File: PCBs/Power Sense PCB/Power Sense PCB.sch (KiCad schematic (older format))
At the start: 84 parts, among them J1 Jack-DC, J10 Test Conn, J2 PWR_INV, J3 PWR_INPUT, J4 PHASE_A_INV, J5 PHASE_A_MOTOR, J6 PHASE_B_INV, J7 PHASE_B_MOTOR, J8 PHASE_C_INV, J9 PHASE_C_MOTOR, U1 INA240A1D, U2 INA240A1D, U3 INA240A1D, U4 INA240A1D

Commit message: Layout + Routing
- Added 5V LED indicatior
- Added 330uF bulk cap on 5V rail
- Changed 8pin to 9pin header (added ground)
- Completed all layout and routing!
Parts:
- added C17: 330uF, Capacitors_THT:CP_Radial_D8.0mm_P3.50mm, symbol Device:CP1
- added D1: RED, LEDs:LED_0603, symbol Device:LED
- added R20: 330, Resistors_SMD:R_0603, symbol Device:R_Small_US
- J10: footprint Pin_Headers:Pin_Header_Straight_1x08_Pitch2.54mm -> Pin_Headers:Pin_Header_Straight_1x09_Pitch2.54mm; symbol Connector_Generic:Conn_01x08 -> Connector_Generic:Conn_01x09; Digikey 961108-6404-AR -> 3M9457-09-ND
- NT1, NT2, NT3, NT4, NT5, NT6, NT7, NT8: footprint NetTies:NetTie-2_SMD_Pad0.5mm -> Power Sense PCB:NetTie-2_SMD_Pad0.25mm
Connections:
- net +5V: now also C17.1, D1.2 (A)
- net GND: now also J10.9 (Pin_9), C17.2, R20.2
- new net: D1.1 (K), R20.1
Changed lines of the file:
@@
 F 0 "NT4" V 3950 1919 50  0000 L CNN
 F 1 "Net-Tie_2" V 3995 1919 50  0001 L CNN
-F 2 "NetTies:NetTie-2_SMD_Pad0.5mm" H 3950 1875 50  0001 C CNN
+F 2 "Power Sense PCB:NetTie-2_SMD_Pad0.25mm" H 3950 1875 50  0001 C CNN
 F 3 "~" H 3950 1875 50  0001 C CNN
 	1    3950 1875
@@
 F 0 "NT3" V 3350 1919 50  0000 L CNN
 F 1 "Net-Tie_2" V 3395 1919 50  0001 L CNN
-F 2 "NetTies:NetTie-2_SMD_Pad0.5mm" H 3350 1875 50  0001 C CNN
+F 2 "Power Sense PCB:NetTie-2_SMD_Pad0.25mm" H 3350 1875 50  0001 C CNN
 F 3 "~" H 3350 1875 50  0001 C CNN
 	1    3350 1875
@@
 	1400 1150 1625 1150
 Wire Wire Line
-	1625 1150 1625 975
+	1625 1150 1625 1075
 $Comp
 L power:+5V #PWR0103
@@
 	1400 1350 1625 1350
 Wire Wire Line
-	1625 1350 1625 1500
+	1625 1350 1625 1450
 $Comp
 L power:GND #PWR0104
@@
 F 0 "NT6" V 3925 4019 50  0000 L CNN
 F 1 "Net-Tie_2" V 3970 4019 50  0001 L CNN
-F 2 "NetTies:NetTie-2_SMD_Pad0.5mm" H 3925 3975 50  0001 C CNN
+F 2 "Power Sense PCB:NetTie-2_SMD_Pad0.25mm" H 3925 3975 50  0001 C CNN
 F 3 "~" H 3925 3975 50  0001 C CNN
 	1    3925 3975
@@
 F 0 "NT5" V 3325 4019 50  0000 L CNN
 F 1 "Net-Tie_2" V 3370 4019 50  0001 L CNN
-F 2 "NetTies:NetTie-2_SMD_Pad0.5mm" H 3325 3975 50  0001 C CNN
+F 2 "Power Sense PCB:NetTie-2_SMD_Pad0.25mm" H 3325 3975 50  0001 C CNN
 F 3 "~" H 3325 3975 50  0001 C CNN
 	1    3325 3975
@@
 F 0 "NT8" V 3900 6094 50  0000 L CNN
 F 1 "Net-Tie_2" V 3945 6094 50  0001 L CNN
-F 2 "NetTies:NetTie-2_SMD_Pad0.5mm" H 3900 6050 50  0001 C CNN
+F 2 "Power Sense PCB:NetTie-2_SMD_Pad0.25mm" H 3900 6050 50  0001 C CNN
 F 3 "~" H 3900 6050 50  0001 C CNN
 	1    3900 6050
@@
 F 0 "NT7" V 3300 6094 50  0000 L CNN
 F 1 "Net-Tie_2" V 3345 6094 50  0001 L CNN
-F 2 "NetTies:NetTie-2_SMD_Pad0.5mm" H 3300 6050 50  0001 C CNN
+F 2 "Power Sense PCB:NetTie-2_SMD_Pad0.25mm" H 3300 6050 50  0001 C CNN
 F 3 "~" H 3300 6050 50  0001 C CNN
 	1    3300 6050
@@
 F 0 "NT2" V 8175 1844 50  0000 L CNN
 F 1 "Net-Tie_2" V 8220 1844 50  0001 L CNN
-F 2 "NetTies:NetTie-2_SMD_Pad0.5mm" H 8175 1800 50  0001 C CNN
+F 2 "Power Sense PCB:NetTie-2_SMD_Pad0.25mm" H 8175 1800 50  0001 C CNN
 F 3 "~" H 8175 1800 50  0001 C CNN
 	1    8175 1800
@@
 F 0 "NT1" V 7575 1844 50  0000 L CNN
 F 1 "Net-Tie_2" V 7620 1844 50  0001 L CNN
-F 2 "NetTies:NetTie-2_SMD_Pad0.5mm" H 7575 1800 50  0001 C CNN
+F 2 "Power Sense PCB:NetTie-2_SMD_Pad0.25mm" H 7575 1800 50  0001 C CNN
 F 3 "~" H 7575 1800 50  0001 C CNN
 	1    7575 1800
@@
 Should be approx the same\nvoltage as the real motor neutral, \nsince phases are close to balanced.
 $Comp
-L Connector_Generic:Conn_01x08 J10
+L Connector_Generic:Conn_01x09 J10
 U 1 1 5E4D3815
 P 10550 3700
-F 0 "J10" H 10475 4100 50  0000 L CNN
+F 0 "J10" H 10500 4225 50  0000 L CNN
 F 1 "Test Conn" H 10475 3200 50  0000 L CNN
-F 2 "Pin_Headers:Pin_Header_Straight_1x08_Pitch2.54mm" H 10550 3700 50  0001 C CNN
+F 2 "Pin_Headers:Pin_Header_Straight_1x09_Pitch2.54mm" H 10550 3700 50  0001 C CNN
 F 3 "~" H 10550 3700 50  0001 C CNN
-F 4 "961108-6404-AR" H 10550 3700 50  0001 C CNN "Digikey"
+F 4 "3M9457-09-ND" H 10550 3700 50  0001 C CNN "Digikey"
 	1    10550 3700
 	1    0    0    -1
 $EndComp
 Wire Wire Line
+	10350 3300 9825 3300
+Wire Wire Line
 	10350 3400 9825 3400
-Wire Wire Line
-	10350 3500 9825 3500
+Text Label 9825 3300 0    50   ~ 0
+V_BUS
 Text Label 9825 3400 0    50   ~ 0
-V_BUS
-Text Label 9825 3500 0    50   ~ 0
 I_BUS
 Wire Wire Line
-	9825 3600 10350 3600
+	9825 3500 10350 3500
+Wire Wire Line
+	10350 3600 9825 3600
 Wire Wire Line
 	10350 3700 9825 3700
@@
 Wire Wire Line
 	10350 4000 9825 4000
-Wire Wire Line
-	10350 4100 9825 4100
 $Comp
 L Device:C_Small C7
@@
 Wire Wire Line
 	6250 3900 7200 3900
+Text Label 9825 3500 0    50   ~ 0
+V_PHASE_A
 Text Label 9825 3600 0    50   ~ 0
-V_PHASE_A
+V_PHASE_B
 Text Label 9825 3700 0    50   ~ 0
-V_PHASE_B
+V_PHASE_C
+Text Label 9825 3900 0    50   ~ 0
+I_PHASE_B
 Text Label 9825 3800 0    50   ~ 0
-V_PHASE_C
+I_PHASE_A
 Text Label 9825 4000 0    50   ~ 0
-I_PHASE_B
-Text Label 9825 3900 0    50   ~ 0
-I_PHASE_A
-Text Label 9825 4100 0    50   ~ 0
 I_PHASE_C
-Text Notes 9550 4375 0    50   ~ 0
+Text Notes 9525 4600 0    50   ~ 0
 For data aquistion via Arduino or similar.
-Text Notes 10025 4500 0    50   ~ 0
+Text Notes 10000 4725 0    50   ~ 0
 All signals 0-5V
 $Comp
@@
 Wire Wire Line
 	7125 1625 7575 1625
+$Comp
+L Device:CP1 C17
+U 1 1 5E383FE4
+P 1800 1250
+F 0 "C17" H 1915 1296 50  0000 L CNN
+F 1 "330uF" H 1915 1205 50  0000 L CNN
+F 2 "Capacitors_THT:CP_Radial_D8.0mm_P3.50mm" H 1800 1250 50  0001 C CNN
+F 3 "~" H 1800 1250 50  0001 C CNN
+F 4 "493-15427-ND" H 1800 1250 50  0001 C CNN "Digikey"
+	1    1800 1250
+	1    0    0    -1
+$EndComp
+Wire Wire Line
+	1625 1075 1800 1075
+Wire Wire Line
+	1800 1075 1800 1100
+Connection ~ 1625 1075
+Wire Wire Line
+	1625 1075 1625 975
+Wire Wire Line
+	1800 1400 1800 1450
+Wire Wire Line
+	1800 1450 1625 1450
+Connection ~ 1625 1450
+Wire Wire Line
+	1625 1450 1625 1500
+$Comp
+L Device:LED D1
+U 1 1 5E3AA4EA
+P 2225 1250
+F 0 "D1" V 2264 1132 50  0000 R CNN
+F 1 "RED" V 2173 1132 50  0000 R CNN
+F 2 "LEDs:LED_0603" H 2225 1250 50  0001 C CNN
+F 3 "~" H 2225 1250 50  0001 C CNN
+F 4 "160-1447-1-ND" V 2225 1250 50  0001 C CNN "Digikey"
+	1    2225 1250
+	0    -1   -1   0
+$EndComp
+Wire Wire Line
+	1800 1075 2225 1075
+Wire Wire Line
+	2225 1075 2225 1100
+Connection ~ 1800 1075
+$Comp
+L Device:R_Small_US R20
+U 1 1 5E3B8A0C
+P 2225 1550
+F 0 "R20" H 2293 1596 50  0000 L CNN
+F 1 "330" H 2293 1505 50  0000 L CNN
+F 2 "Resistors_SMD:R_0603" H 2225 1550 50  0001 C CNN
+F 3 "~" H 2225 1550 50  0001 C CNN
+F 4 "RHM330DCT-ND" H 2225 1550 50  0001 C CNN "Digikey"
+	1    2225 1550
+	1    0    0    -1
+$EndComp
+Wire Wire Line
+	2225 1400 2225 1450
+Wire Wire Line
+	2225 1650 2225 1725
+$Comp
+L power:GND #PWR01
+U 1 1 5E3D3814
+P 2225 1725
+F 0 "#PWR01" H 2225 1475 50  0001 C CNN
+F 1 "GND" H 2230 1552 50  0000 C CNN
+F 2 "" H 2225 1725 50  0001 C CNN
+F 3 "" H 2225 1725 50  0001 C CNN
+	1    2225 1725
+	1    0    0    -1
+$EndComp
+Wire Wire Line
+	10350 4100 10275 4100
+Wire Wire Line
+	10275 4100 10275 4175
+$Comp
+L power:GND #PWR?
+U 1 1 5E454E34
+P 10275 4175
+F 0 "#PWR?" H 10275 3925 50  0001 C CNN
+F 1 "GND" H 10280 4002 50  0000 C CNN
+F 2 "" H 10275 4175 50  0001 C CNN
+F 3 "" H 10275 4175 50  0001 C CNN
+	1    10275 4175
+	1    0    0    -1
+$EndComp
 $EndSCHEMATC

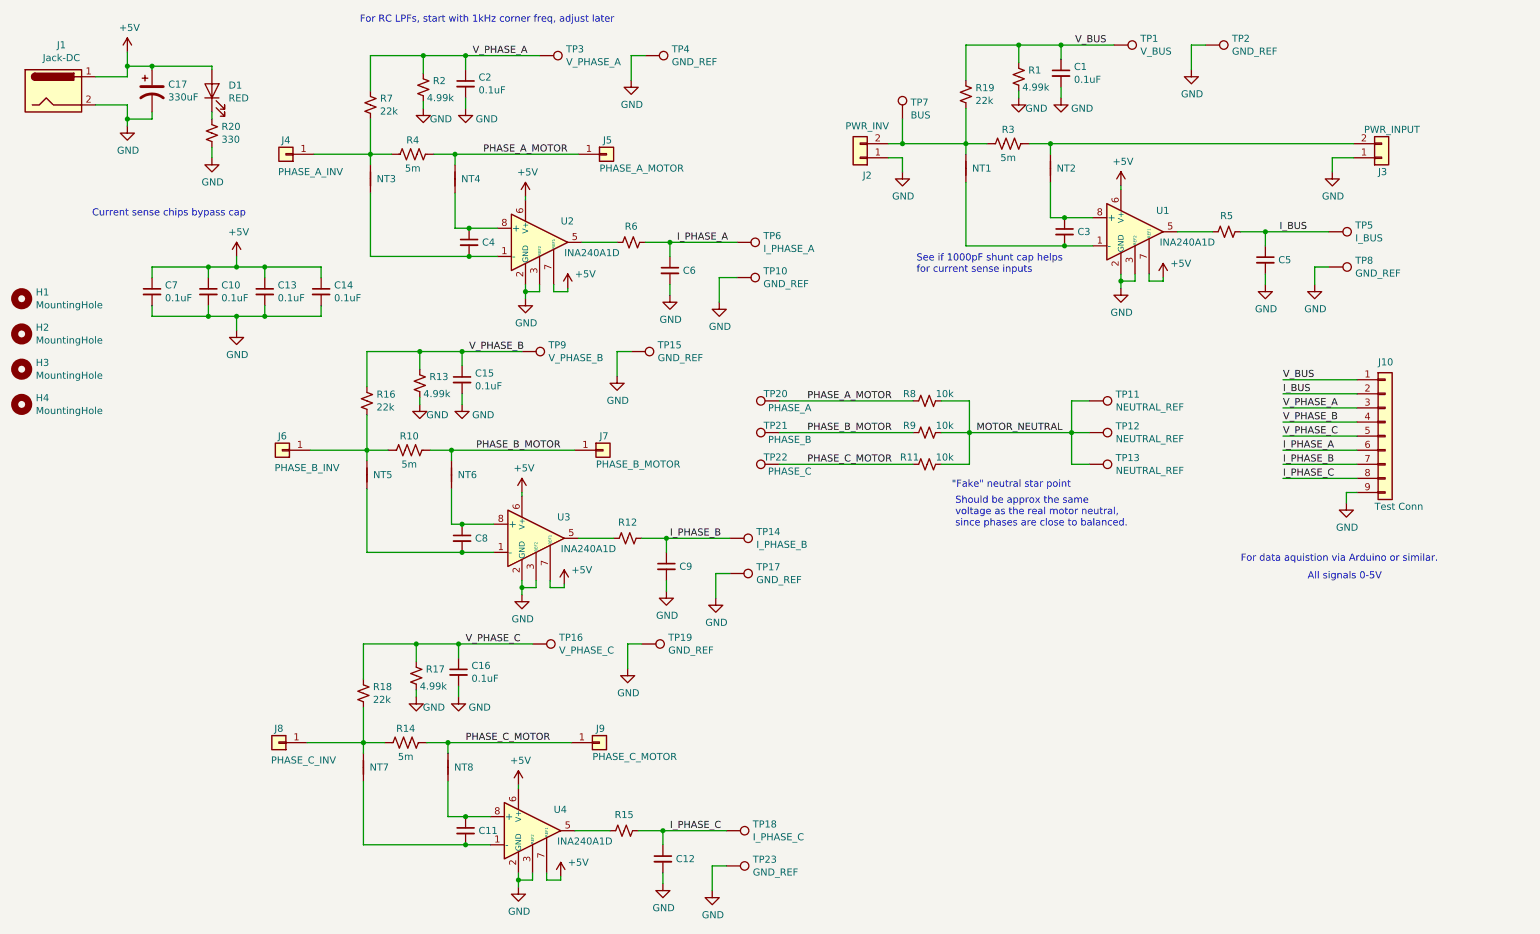
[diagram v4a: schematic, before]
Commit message: Gerbers and Small Changes
- Swapped Ref1 and Ref2 values based on datasheet (doesn't matter really)
- Updated Silkscreen
- Exported Gerbers
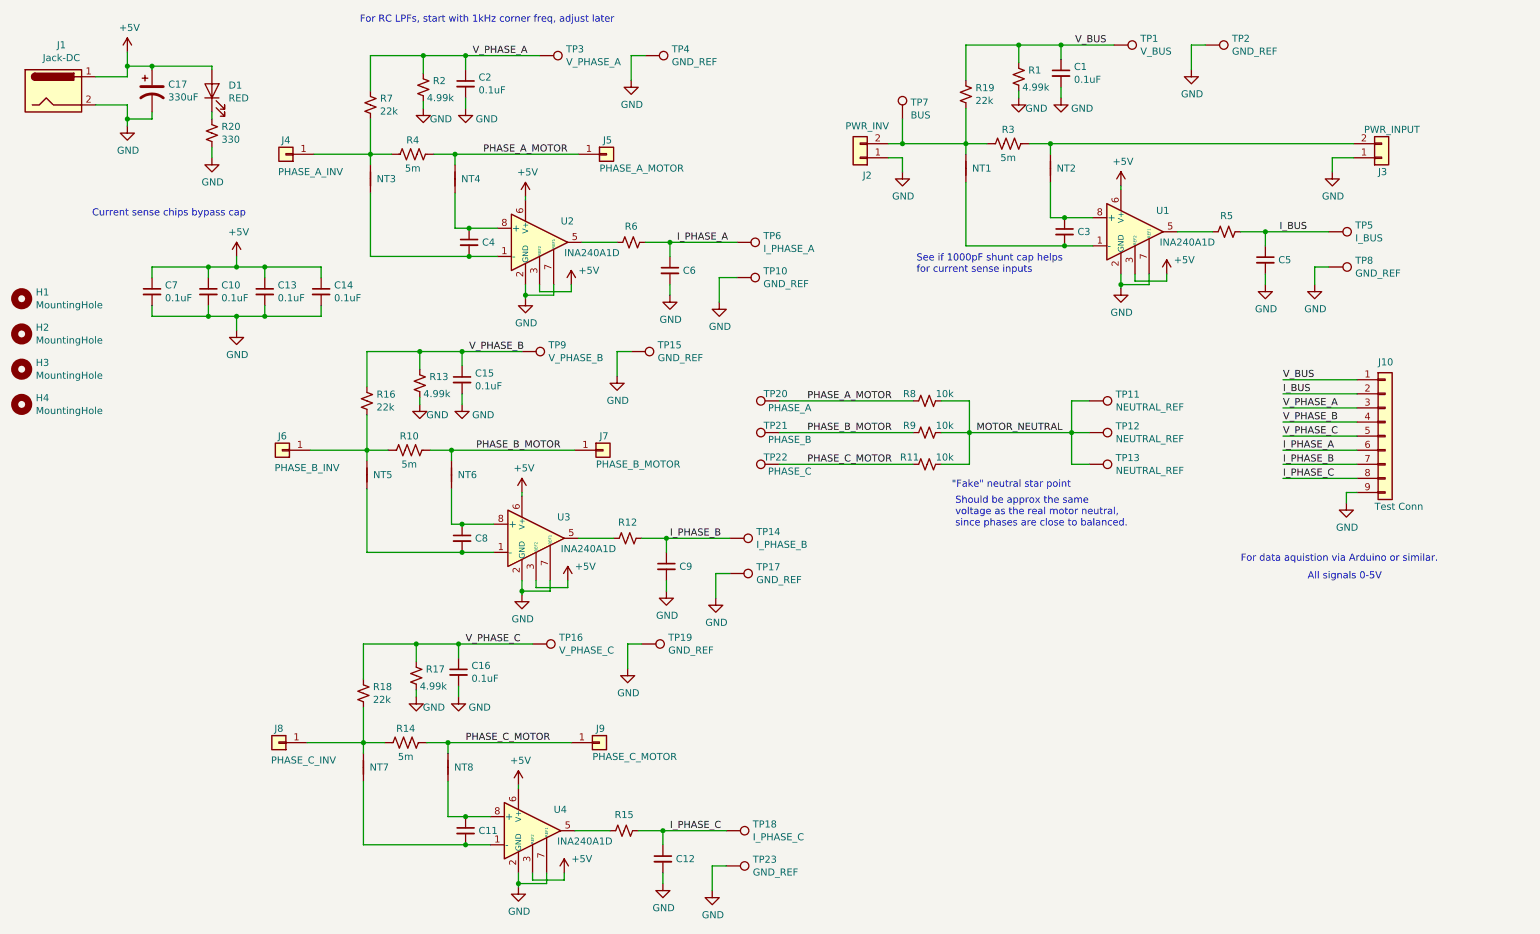
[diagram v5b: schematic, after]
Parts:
- U1, U2, U3, U4: footprint Housings_SOIC:SOIC-8-1EP_3.9x4.9mm_Pitch1.27mm -> Housings_SOIC:SOIC-8_3.9x4.9mm_Pitch1.27mm
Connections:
- net +5V: now also U1.3 (REF2), U2.3 (REF2), U3.3 (REF2), U4.3 (REF2); no longer U1.7 (REF1), U2.7 (REF1), U3.7 (REF1), U4.7 (REF1)
- net GND: now also U1.7 (REF1), U2.7 (REF1), U3.7 (REF1), U4.7 (REF1); no longer U1.3 (REF2), U2.3 (REF2), U3.3 (REF2), U4.3 (REF2)
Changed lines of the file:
@@
 Wire Wire Line
 	4450 2025 4450 2000
-Wire Wire Line
-	4450 2625 4450 2675
 $Comp
 L power:+5V #PWR0101
@@
 	1625 1350 1625 1450
 $Comp
-L power:GND #PWR0104
-U 1 1 5E2A5BAB
-P 4450 2725
-F 0 "#PWR0104" H 4450 2475 50  0001 C CNN
-F 1 "GND" H 4455 2552 50  0000 C CNN
-F 2 "" H 4450 2725 50  0001 C CNN
-F 3 "" H 4450 2725 50  0001 C CNN
-	1    4450 2725
-	1    0    0    -1
-$EndComp
-$Comp
 L power:GND #PWR0105
 U 1 1 5E2A60B1
@@
 F 3 "" H 1625 1500 50  0001 C CNN
 	1    1625 1500
-	1    0    0    -1
-$EndComp
-Wire Wire Line
-	4550 2625 4550 2675
-Wire Wire Line
-	4550 2675 4450 2675
-Connection ~ 4450 2675
-Wire Wire Line
-	4450 2675 4450 2725
-Wire Wire Line
-	4650 2625 4650 2675
-Wire Wire Line
-	4650 2675 4750 2675
-Wire Wire Line
-	4750 2675 4750 2650
-$Comp
-L power:+5V #PWR0106
-U 1 1 5E2A7916
-P 4750 2650
-F 0 "#PWR0106" H 4750 2500 50  0001 C CNN
-F 1 "+5V" H 4875 2750 50  0000 C CNN
-F 2 "" H 4750 2650 50  0001 C CNN
-F 3 "" H 4750 2650 50  0001 C CNN
-	1    4750 2650
 	1    0    0    -1
 $EndComp
@@
 Wire Wire Line
 	4425 4125 4425 4100
-Wire Wire Line
-	4425 4725 4425 4775
 $Comp
 L power:+5V #PWR0110
@@
 	0    1    1    0
 $EndComp
-$Comp
-L power:GND #PWR0112
-U 1 1 5E2DD8E3
-P 4425 4825
-F 0 "#PWR0112" H 4425 4575 50  0001 C CNN
-F 1 "GND" H 4430 4652 50  0000 C CNN
-F 2 "" H 4425 4825 50  0001 C CNN
-F 3 "" H 4425 4825 50  0001 C CNN
-	1    4425 4825
-	1    0    0    -1
-$EndComp
-Wire Wire Line
-	4525 4725 4525 4775
-Wire Wire Line
-	4525 4775 4425 4775
-Connection ~ 4425 4775
-Wire Wire Line
-	4425 4775 4425 4825
-Wire Wire Line
-	4625 4725 4625 4775
-Wire Wire Line
-	4625 4775 4725 4775
-Wire Wire Line
-	4725 4775 4725 4750
-$Comp
-L power:+5V #PWR0113
-U 1 1 5E2DD8F0
-P 4725 4750
-F 0 "#PWR0113" H 4725 4600 50  0001 C CNN
-F 1 "+5V" H 4850 4850 50  0000 C CNN
-F 2 "" H 4725 4750 50  0001 C CNN
-F 3 "" H 4725 4750 50  0001 C CNN
-	1    4725 4750
-	1    0    0    -1
-$EndComp
 Wire Wire Line
 	2925 3800 3325 3800
@@
 Wire Wire Line
 	4400 6200 4400 6175
-Wire Wire Line
-	4400 6800 4400 6850
 $Comp
 L power:+5V #PWR0117
@@
 	0    1    1    0
 $EndComp
-$Comp
-L power:GND #PWR0119
-U 1 1 5E2FB61A
-P 4400 6900
-F 0 "#PWR0119" H 4400 6650 50  0001 C CNN
-F 1 "GND" H 4405 6727 50  0000 C CNN
-F 2 "" H 4400 6900 50  0001 C CNN
-F 3 "" H 4400 6900 50  0001 C CNN
-	1    4400 6900
-	1    0    0    -1
-$EndComp
-Wire Wire Line
-	4500 6800 4500 6850
-Wire Wire Line
-	4500 6850 4400 6850
-Connection ~ 4400 6850
-Wire Wire Line
-	4400 6850 4400 6900
-Wire Wire Line
-	4600 6800 4600 6850
-Wire Wire Line
-	4600 6850 4700 6850
-Wire Wire Line
-	4700 6850 4700 6825
-$Comp
-L power:+5V #PWR0120
-U 1 1 5E2FB627
-P 4700 6825
-F 0 "#PWR0120" H 4700 6675 50  0001 C CNN
-F 1 "+5V" H 4825 6925 50  0000 C CNN
-F 2 "" H 4700 6825 50  0001 C CNN
-F 3 "" H 4700 6825 50  0001 C CNN
-	1    4700 6825
-	1    0    0    -1
-$EndComp
 Wire Wire Line
 	2900 5875 3300 5875
@@
 Wire Wire Line
 	8675 1950 8675 1925
-Wire Wire Line
-	8675 2550 8675 2600
 $Comp
 L power:+5V #PWR0124
@@
 Wire Wire Line
 	8775 2550 8775 2600
-Wire Wire Line
-	8775 2600 8675 2600
-Connection ~ 8675 2600
-Wire Wire Line
-	8675 2600 8675 2650
-Wire Wire Line
-	8875 2550 8875 2600
-Wire Wire Line
-	8875 2600 8975 2600
-Wire Wire Line
-	8975 2600 8975 2575
 $Comp
 L power:+5V #PWR0127
 U 1 1 5E3A5FDF
-P 8975 2575
-F 0 "#PWR0127" H 8975 2425 50  0001 C CNN
-F 1 "+5V" H 9100 2675 50  0000 C CNN
-F 2 "" H 8975 2575 50  0001 C CNN
-F 3 "" H 8975 2575 50  0001 C CNN
-	1    8975 2575
+P 9000 2550
+F 0 "#PWR0127" H 9000 2400 50  0001 C CNN
+F 1 "+5V" H 9125 2650 50  0000 C CNN
+F 2 "" H 9000 2550 50  0001 C CNN
+F 3 "" H 9000 2550 50  0001 C CNN
+	1    9000 2550
 	1    0    0    -1
 $EndComp
@@
 F 0 "U2" H 4700 2475 50  0000 L CNN
 F 1 "INA240A1D" H 4725 2250 50  0000 L CNN
-F 2 "Housings_SOIC:SOIC-8-1EP_3.9x4.9mm_Pitch1.27mm" H 4550 1675 50  0001 C CNN
+F 2 "Housings_SOIC:SOIC-8_3.9x4.9mm_Pitch1.27mm" H 4550 1675 50  0001 C CNN
 F 3 "http://www.ti.com/lit/ds/symlink/ina240.pdf" H 4700 2475 50  0001 C CNN
 F 4 "296-49646-1-ND" H 4550 2325 50  0001 C CNN "Digikey"
@@
 F 0 "U1" H 8925 2400 50  0000 L CNN
 F 1 "INA240A1D" H 8950 2175 50  0000 L CNN
-F 2 "Housings_SOIC:SOIC-8-1EP_3.9x4.9mm_Pitch1.27mm" H 8775 1600 50  0001 C CNN
+F 2 "Housings_SOIC:SOIC-8_3.9x4.9mm_Pitch1.27mm" H 8775 1600 50  0001 C CNN
 F 3 "http://www.ti.com/lit/ds/symlink/ina240.pdf" H 8925 2400 50  0001 C CNN
 F 4 "296-49646-1-ND" H 8775 2250 50  0001 C CNN "Digikey"
@@
 F 0 "U3" H 4675 4575 50  0000 L CNN
 F 1 "INA240A1D" H 4700 4350 50  0000 L CNN
-F 2 "Housings_SOIC:SOIC-8-1EP_3.9x4.9mm_Pitch1.27mm" H 4525 3775 50  0001 C CNN
+F 2 "Housings_SOIC:SOIC-8_3.9x4.9mm_Pitch1.27mm" H 4525 3775 50  0001 C CNN
 F 3 "http://www.ti.com/lit/ds/symlink/ina240.pdf" H 4675 4575 50  0001 C CNN
 F 4 "296-49646-1-ND" H 4525 4425 50  0001 C CNN "Digikey"
@@
 F 0 "U4" H 4650 6650 50  0000 L CNN
 F 1 "INA240A1D" H 4675 6425 50  0000 L CNN
-F 2 "Housings_SOIC:SOIC-8-1EP_3.9x4.9mm_Pitch1.27mm" H 4500 5850 50  0001 C CNN
+F 2 "Housings_SOIC:SOIC-8_3.9x4.9mm_Pitch1.27mm" H 4500 5850 50  0001 C CNN
 F 3 "http://www.ti.com/lit/ds/symlink/ina240.pdf" H 4650 6650 50  0001 C CNN
 F 4 "296-49646-1-ND" H 4500 6500 50  0001 C CNN "Digikey"
@@
 	10275 4100 10275 4175
 $Comp
-L power:GND #PWR?
+L power:GND #PWR0139
 U 1 1 5E454E34
 P 10275 4175
-F 0 "#PWR?" H 10275 3925 50  0001 C CNN
+F 0 "#PWR0139" H 10275 3925 50  0001 C CNN
 F 1 "GND" H 10280 4002 50  0000 C CNN
 F 2 "" H 10275 4175 50  0001 C CNN
@@
 	1    0    0    -1
 $EndComp
+Wire Wire Line
+	8675 2550 8675 2625
+Wire Wire Line
+	8675 2625 8875 2625
+Connection ~ 8675 2625
+Wire Wire Line
+	8675 2625 8675 2650
+Wire Wire Line
+	8875 2550 8875 2625
+Wire Wire Line
+	8775 2600 9000 2600
+Wire Wire Line
+	9000 2600 9000 2550
+$Comp
+L power:GND #PWR0104
+U 1 1 5E590FFB
+P 4450 2725
+F 0 "#PWR0104" H 4450 2475 50  0001 C CNN
+F 1 "GND" H 4455 2552 50  0000 C CNN
+F 2 "" H 4450 2725 50  0001 C CNN
+F 3 "" H 4450 2725 50  0001 C CNN
+	1    4450 2725
+	1    0    0    -1
+$EndComp
+Wire Wire Line
+	4550 2625 4550 2675
+$Comp
+L power:+5V #PWR0106
+U 1 1 5E591002
+P 4775 2625
+F 0 "#PWR0106" H 4775 2475 50  0001 C CNN
+F 1 "+5V" H 4900 2725 50  0000 C CNN
+F 2 "" H 4775 2625 50  0001 C CNN
+F 3 "" H 4775 2625 50  0001 C CNN
+	1    4775 2625
+	1    0    0    -1
+$EndComp
+Wire Wire Line
+	4450 2625 4450 2700
+Wire Wire Line
+	4450 2700 4650 2700
+Connection ~ 4450 2700
+Wire Wire Line
+	4450 2700 4450 2725
+Wire Wire Line
+	4650 2625 4650 2700
+Wire Wire Line
+	4550 2675 4775 2675
+Wire Wire Line
+	4775 2675 4775 2625
+$Comp
+L power:GND #PWR0112
+U 1 1 5E5A9F38
+P 4425 4825
+F 0 "#PWR0112" H 4425 4575 50  0001 C CNN
+F 1 "GND" H 4430 4652 50  0000 C CNN
+F 2 "" H 4425 4825 50  0001 C CNN
+F 3 "" H 4425 4825 50  0001 C CNN
+	1    4425 4825
+	1    0    0    -1
+$EndComp
+Wire Wire Line
+	4525 4725 4525 4775
+$Comp
+L power:+5V #PWR0113
+U 1 1 5E5A9F3F
+P 4750 4725
+F 0 "#PWR0113" H 4750 4575 50  0001 C CNN
+F 1 "+5V" H 4875 4825 50  0000 C CNN
+F 2 "" H 4750 4725 50  0001 C CNN
+F 3 "" H 4750 4725 50  0001 C CNN
+	1    4750 4725
+	1    0    0    -1
+$EndComp
+Wire Wire Line
+	4425 4725 4425 4800
+Wire Wire Line
+	4425 4800 4625 4800
+Connection ~ 4425 4800
+Wire Wire Line
+	4425 4800 4425 4825
+Wire Wire Line
+	4625 4725 4625 4800
+Wire Wire Line
+	4525 4775 4750 4775
+Wire Wire Line
+	4750 4775 4750 4725
+$Comp
+L power:GND #PWR0119
+U 1 1 5E5C29FF
+P 4400 6900
+F 0 "#PWR0119" H 4400 6650 50  0001 C CNN
+F 1 "GND" H 4405 6727 50  0000 C CNN
+F 2 "" H 4400 6900 50  0001 C CNN
+F 3 "" H 4400 6900 50  0001 C CNN
+	1    4400 6900
+	1    0    0    -1
+$EndComp
+Wire Wire Line
+	4500 6800 4500 6850
+$Comp
+L power:+5V #PWR0120
+U 1 1 5E5C2A06
+P 4725 6800
+F 0 "#PWR0120" H 4725 6650 50  0001 C CNN
+F 1 "+5V" H 4850 6900 50  0000 C CNN
+F 2 "" H 4725 6800 50  0001 C CNN
+F 3 "" H 4725 6800 50  0001 C CNN
+	1    4725 6800
+	1    0    0    -1
+$EndComp
+Wire Wire Line
+	4400 6800 4400 6875
+Wire Wire Line
+	4400 6875 4600 6875
+Connection ~ 4400 6875
+Wire Wire Line
+	4400 6875 4400 6900
+Wire Wire Line
+	4600 6800 4600 6875
+Wire Wire Line
+	4500 6850 4725 6850
+Wire Wire Line
+	4725 6850 4725 6800
 $EndSCHEMATC
